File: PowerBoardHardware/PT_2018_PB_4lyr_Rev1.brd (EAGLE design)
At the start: 177.8 x 209.6 mm, 249 parts, among them J1 APP_2POS_CONFIG12V_VERT, J2 APP_2POS_CONFIG12V_VERT, J3 APP_2POS_CONFIG12V_VERT, J4 RJ45KEYSTONE-942, J5 APP_2POS_CONFIGMOCO_VERT, J6 JTAG_ARM_10PIN, Q1 Q_IRFS7437PbF, Q10 Q_IRFS7437PbF, Q11 2N7002, Q12 2N7002, Q13 2N7002PW, Q2 Q_IRFS7437PbF, Q3 Q_IRFS7437PbF, Q4 Q_IRFS7437PbF, Q5 MOSFET-NCHANNELFDD8780, Q6 Q_IRFS7437PbF, Q7 Q_IRFS7437PbF, Q8 MOSFET-NCHANNELFDD8780, Q9 Q_IRFS7437PbF, U1 ACS722LLCTR-40AU-T, U10 LT1910, U11 LT1910, U12 ACS722LLCTR-40AU-T, U13 LT1910, U14 ACS722LLCTR-40AU-T, U15 LT1910, U16 LT1910, U17 ACS722LLCTR-40AU-T, U18 ACS722LLCTR-40AU-T, U19 LT1910, U2 ACS722LLCTR-40AU-T, U20 LT1910, U21 SLVU2.8-4, U22 HX1198FNL, U23 MAX3232D, U3 LT1910, U4 ACS722LLCTR-40AU-T, U5 LT1910, U6 ACS722LLCTR-40AU-T, U7 LT1910, U8 ACS722LLCTR-40AU-T, U9 ACS722LLCTR-40AU-T, Y1 CRYATL_32K_SMD, Y2 NX3225GA

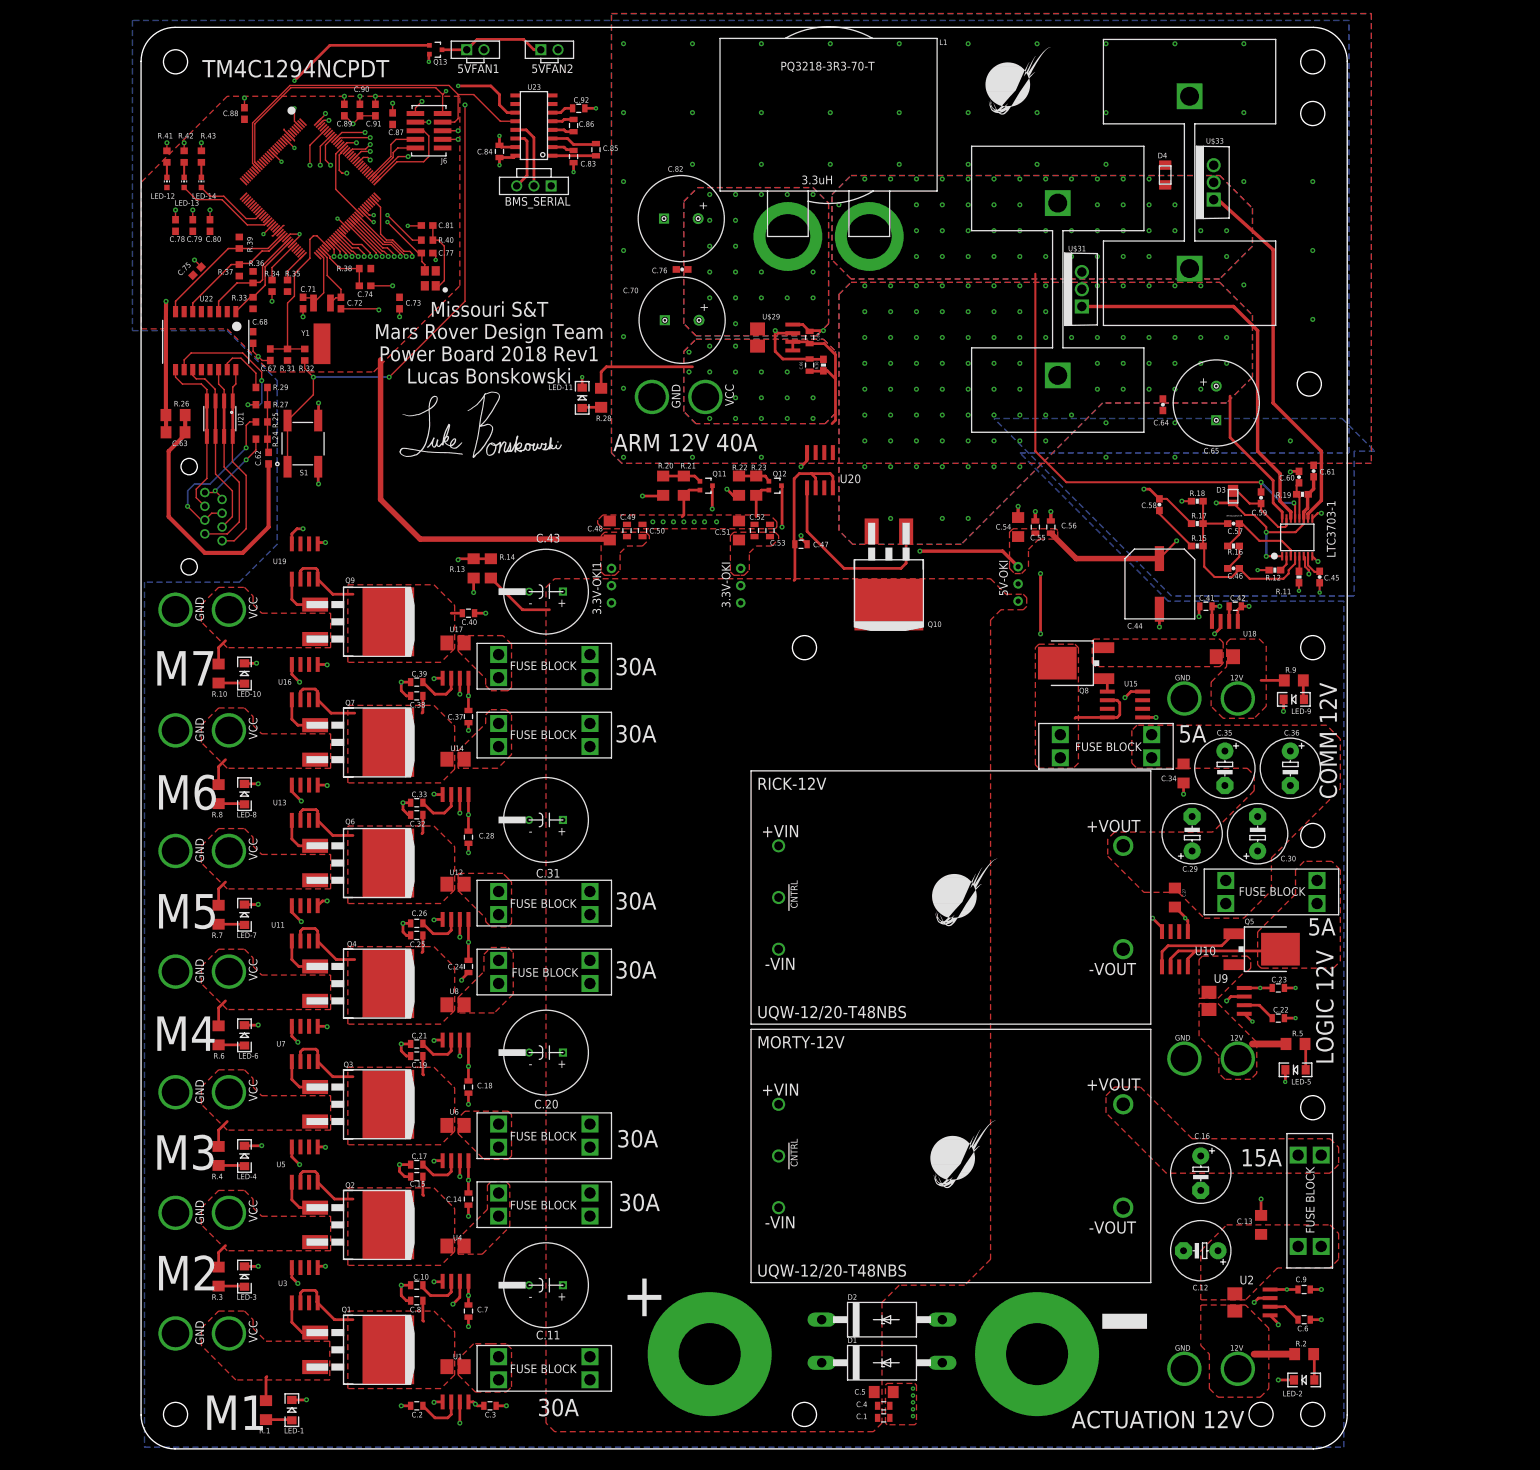
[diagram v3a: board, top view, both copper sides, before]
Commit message: Rev 2 2018
Integrated tiva/ buck converter removed.  Pack voltage arm bus added. Positive and negative terminals flipped.  Could add pin receptacles to muratas still
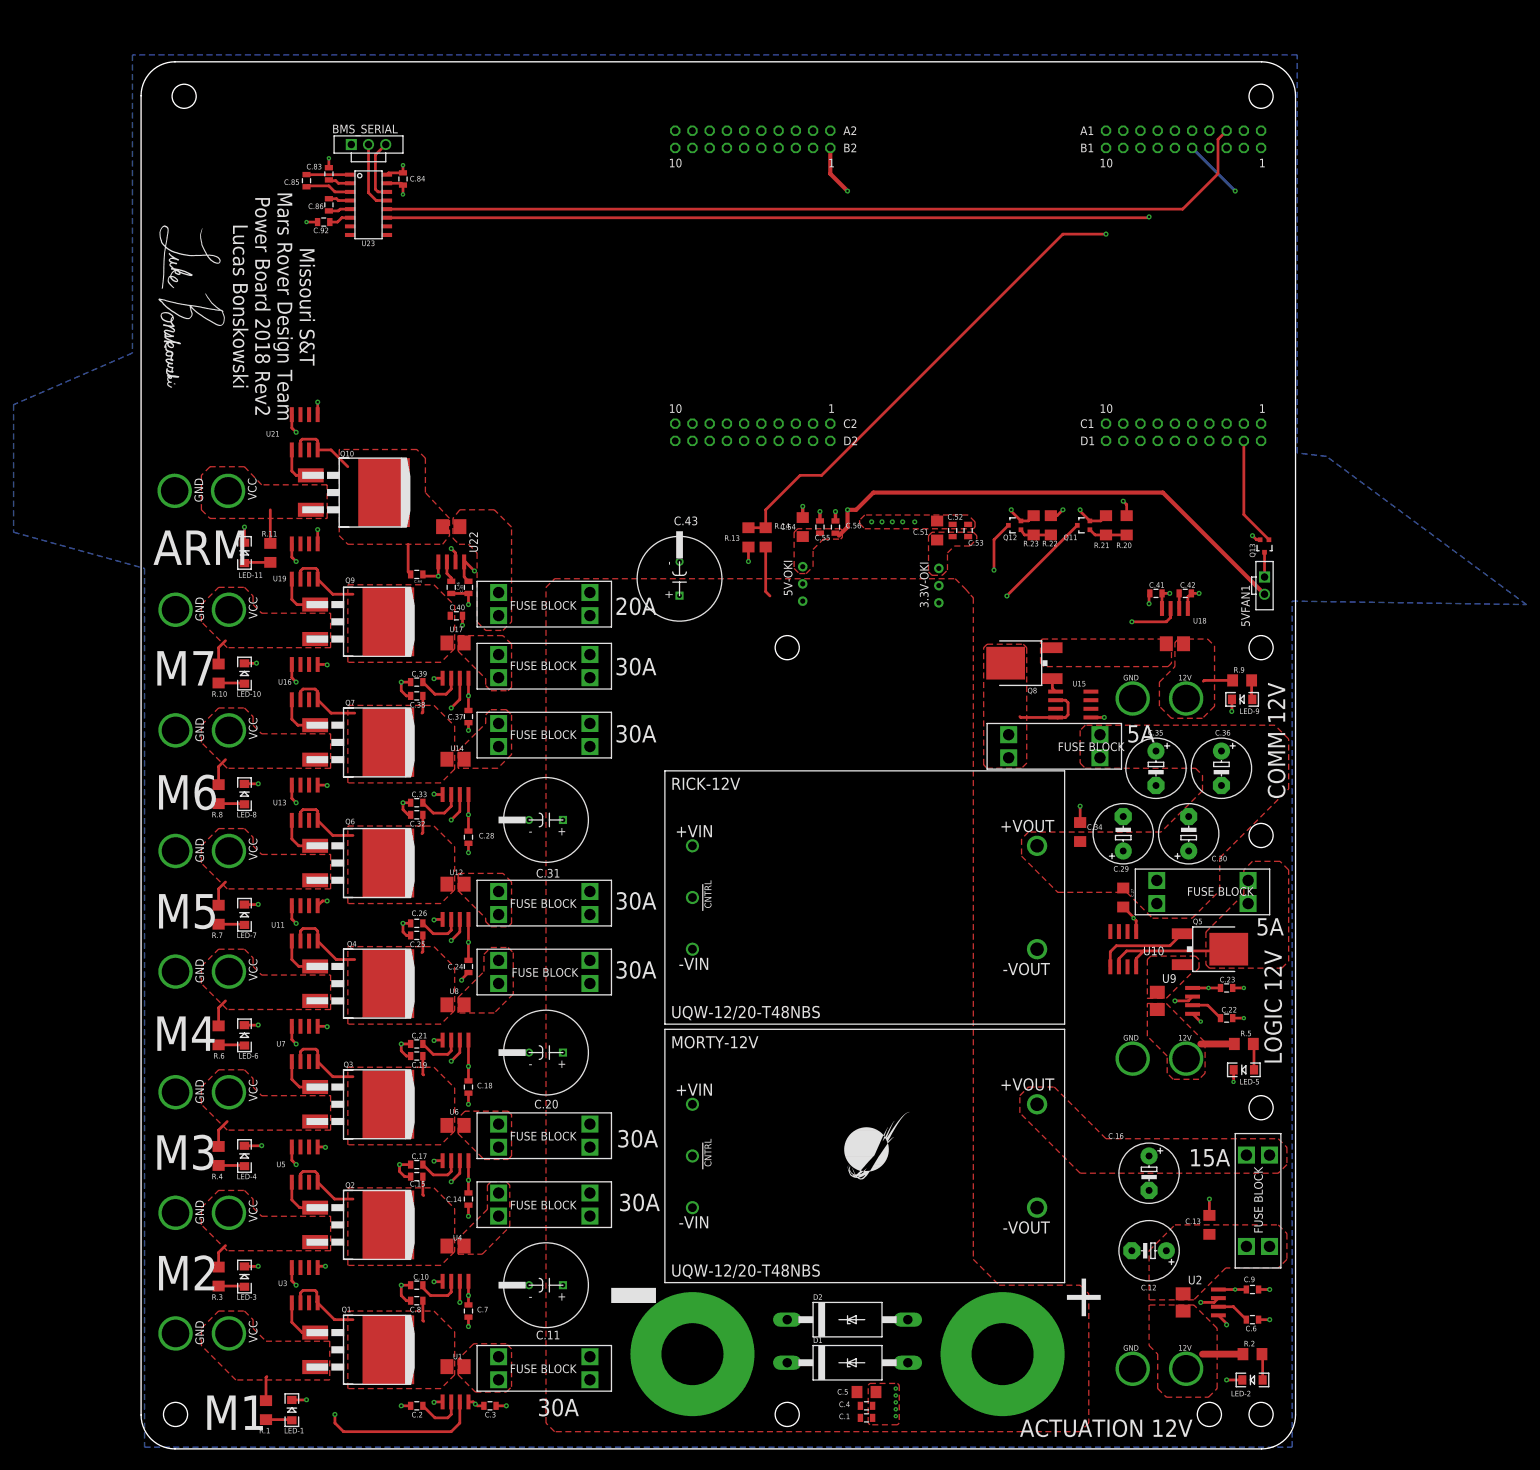
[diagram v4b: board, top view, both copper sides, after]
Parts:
- removed 3.3V-OKI1: Q_OKI-78SR, MRDT-2015-PowerBoard:OKI-78SR_HORIZ
- removed 5VFAN2: SL02, MRDT-Connectors:MOLEX-70543-0001
- removed C.47, C.69: .1µF, SparkFun-Capacitors:0805
- removed C.48: 10uF, SparkFun-Capacitors:1206
- removed C.49: 1nF, SparkFun-Capacitors:0805
- removed C.50: .1uF, SparkFun-Capacitors:0805
- removed C.57: 470p, SparkFun-Passives:0603-CAP
- removed C.58: 2200p, SparkFun-Passives:0603-CAP
- removed C.59: 0.1uF, SparkFun-Passives:0603-CAP
- removed C.60: 1uF, SparkFun-Passives:0603-CAP
- removed C.61: 10u, SparkFun-Passives:0603-CAP
- removed C.62: 1000pF, resistor:C0603
- removed C.63: 4700pF, resistor:C1206
- removed C.64: 1000p, SparkFun-Passives:0603-CAP
- removed C.65: 100u, buckconverter:CAP_POL_220UF
- removed C.66: 10n, SparkFun-Capacitors:0805
- removed C.67, C.68, C.73, C.74, C.75, C.78, C.79, C.80, C.87, C.88, C.90: 0.1uF, resistor:C0603
- removed C.70, C.82: 220u, buckconverter:CAP_POL_220UF
- removed C.71, C.72, C.77, C.81: 12pF, resistor:C0603
- removed C.76: 22p, SparkFun-Passives:0603-CAP
- removed C.89: 2.2uF, resistor:C0603
- removed C.91: 1.0uF, resistor:C0603
- removed D3: RF05VAM1STR, buckconverter:DIODE_STANDARD_100V
- removed D4: RBR3MM30ATR, buckconverter:DIODE_SCHOTTKY_30V_1A
- removed J4: RJ45KEYSTONE-942, MRDT-Connectors:KEYSTONE-942
- removed J5: APP_2POS_CONFIGMOCO_VERT, MRDT-Connectors:APP45_MOCO_VERT_CONFIG
- removed J6: JTAG_ARM_10PIN, MRDT-Connectors:CON_2X5_50MIL
- removed L1: 3.3uH, buckconverter:PLANAR_INDUCTOR_3.3UH
- removed LED-12: ORANGE, led:CHIP-LED0603
- removed LED-13, LED-14: GREEN, led:CHIP-LED0603
- removed LOGO1, U$34: MRDT_LOGO, MRDT-Hardware:MRDT_LOGO
- removed LTC3703-1: LTC3703-5, MRDT-ICs:SSOP-16
- removed R.12: 19.1k, SparkFun-Passives:0603-RES
- removed R.15, R.16, R.30: 10k, SparkFun-Passives:0603-RES
- removed R.17: 113k, SparkFun-Passives:0603-RES
- removed R.18: 8.06k, SparkFun-Passives:0603-RES
- removed R.19: 10, SparkFun-Passives:0603-RES
- removed R.24, R.25, R.27, R.29: 75, resistor:R0603
- removed R.26: 1M, resistor:R1206
- removed R.28: 1kΩ, SparkFun-Passives:1206
- removed R.31: 10k, resistor:R0603
- removed R.32: 100, resistor:R0603
- removed R.33: 49.9, rcl:R0603
- removed R.34: 4.87k 1%, resistor:R0603
- removed R.35: 1M, resistor:R0603
- removed R.36: 49.4, resistor:R0603
- removed R.37, R.39: 49.9, resistor:R0603
- removed R.38: 51, resistor:R0603
- removed R.40: 2k, resistor:R0603
- removed R.41, R.42, R.43: 330, resistor:R0603
- removed S1: SWITCH_TACTILE, MRDT-UserInput:SWITCH_6MM_6MM_TE_CON_SMD
- removed TM4C1294NCPDT: TM4C1294NCPDT, MRDT-Microcontrollers:TQFP-128
- removed U$32: 530002B02500G, buckconverter:RADIAL_FIN_HEATSINK
- removed U$33: IPP052N06L3GXKSA1, buckconverter:TO-220
- removed U$35, U$36, U$37: MOUNTING_HOLE#6, MRDT-Hardware:#6_SCREW
- removed Y1: CRYATL_32K_SMD, MRDT-Passives:CRYSTAL_32K_SMD
- removed Y2: NX3225GA, MRDT-Passives:NDK3.2X2.5
- C.44: value 22u -> .1µF; device buckconverter:CAP_POL_22UF -> SparkFun-Capacitors:0805
- C.45: value 0.1uF -> .1µF; device SparkFun-Passives:0603-CAP -> SparkFun-Capacitors:0805
- C.46: value 1000p -> 1nF; device SparkFun-Passives:0603-CAP -> SparkFun-Capacitors:0805
- R.11: value 16.5k -> 5kΩ; device SparkFun-Passives:0603-RES -> SparkFun-Passives:1206
- U$23: value MOUNTING_HOLE#6 -> APP_2POS_CONFIGMOCO_VERT; device MRDT-Hardware:#6_SCREW -> MRDT-Connectors:APP45_MOCO_VERT_CONFIG
- U$29: value MLX91210 -> ATC_FUSE_BLOCK; device buckconverter:SOIC8_ACS711 -> MRDT-Hardware:BLOCK_3557-2
- U$30: value 530002B02500G -> MOUNTING_HOLE#6; device buckconverter:RADIAL_FIN_HEATSINK -> MRDT-Hardware:#6_SCREW
- U$31: value IPP052N06L3GXKSA1 -> MOUNTING_HOLE#6; device buckconverter:TO-220 -> MRDT-Hardware:#6_SCREW
- U20: value LT1910 -> TIVA-1294; device Jake:SO8 -> MRDT-Microcontrollers:TIVA-C-CONNECTED
- U21: value SLVU2.8-4 -> LT1910; device MRDT-ICs:SOIC8 -> Jake:SO8
- U22: value HX1198FNL -> ACS722LLCTR-40AU-T; device MRDT-ICs:HX1198FNL -> MRDT-2015-PowerBoard:SOIC8_ACS711
- moved R.11 151.7 mm to (19.1, 132.1), turned to 270 degrees
- moved Q13 142.4 mm to (165.6, 133.1), turned to 180 degrees
- moved 5VFAN1 140.6 mm to (165.6, 127.3), turned to 90 degrees
- moved U$30 131.9 mm to (6.35, 199.4), turned to 0 degrees
- moved C.45 125.5 mm to (48.3, 127.0), turned to 90 degrees
- moved C.46 115.3 mm to (45.7, 127.0), turned to 270 degrees
- moved C.44 109.5 mm to (40.6, 128.9), turned to 180 degrees
- moved U$23 99.7 mm to (1.78, 145.2), turned to 270 degrees
- moved Q10 87.4 mm to (29.2, 146.1), turned to 270 degrees
- moved U$28 86.2 mm to (95.2, 118.1)
- moved R.20 68.6 mm to (145.3, 136.1), turned to 90 degrees
- moved R.21 62.5 mm to (142.2, 136.1), turned to 90 degrees
- moved U20 58.3 mm to (41.9, 139.7), turned to 0 degrees
- moved U$29 56.8 mm to (49.5, 127.9), turned to 0 degrees
- moved Q11 55.9 mm to (138.9, 136.1), turned to 90 degrees
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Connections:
- removed net !RESET: J6.P10, R.32.2, S1.P$3, S1.P$4
- removed net +3V3: 3.3V-OKI1.3, C.48.1, C.49.1, C.50.1, C.68.1, C.73.1, C.75.1, C.78.1, C.79.1, C.80.1, C.87.1, C.88.1, J6.P1, LED-12.A, R.31.1, R.33.1, R.35.2, R.36.1, R.37.1, R.38.2, R.39.1, TM4C1294NCPDT.P$101, TM4C1294NCPDT.P$113, TM4C1294NCPDT.P$122, TM4C1294NCPDT.P$16, TM4C1294NCPDT.P$26, TM4C1294NCPDT.P$28, TM4C1294NCPDT.P$39, TM4C1294NCPDT.P$47, TM4C1294NCPDT.P$51, TM4C1294NCPDT.P$52, TM4C1294NCPDT.P$69, TM4C1294NCPDT.P$7, TM4C1294NCPDT.P$79, TM4C1294NCPDT.P$8, TM4C1294NCPDT.P$9, TM4C1294NCPDT.P$90, U22.P$2, U22.P$7
- removed net ARM-BUS: J5.VCC, R.28.1, U$29.4
- removed net EN0LED0: LED-14.A, TM4C1294NCPDT.P$42
- removed net EN0LED1: LED-13.A, TM4C1294NCPDT.P$46
- removed net EN0RXI_N: R.39.2, TM4C1294NCPDT.P$53, U22.P$8
- removed net EN0RXI_P: R.37.2, TM4C1294NCPDT.P$54, U22.P$6
- removed net EN0TXO_N: R.36.2, TM4C1294NCPDT.P$56, U22.P$3
- removed net EN0TXO_P: R.33.2, TM4C1294NCPDT.P$57, U22.P$1
- removed net FAN_CTL_1: Q13.1, TM4C1294NCPDT.P$3
- removed net N$10: LTC3703-1.5, R.11.2
- removed net N$14: C.45.1, LTC3703-1.7
- removed net N$2: LED-11.A, R.28.2
- removed net N$23: C.57.1, LTC3703-1.3, R.16.2
- removed net N$24: C.46.1, R.16.1
- removed net N$26: C.58.1, R.15.1
- removed net N$27: C.46.2, C.57.2, LTC3703-1.4, R.15.2, R.17.2, R.18.1
- removed net N$29: C.60.1, LTC3703-1.12, R.19.1
- removed net N$30: LTC3703-1.10, U$33.1
- removed net N$31: C.59.2, D4.P$2, L1.P$2, LTC3703-1.13, U$31.3, U$33.2
- removed net N$32: C.59.1, D3.P$1, LTC3703-1.15
- removed net N$33: LTC3703-1.14, U$31.1
- removed net N$34: LTC3703-1.2, R.12.2
- removed net N$36: Q10.1, U20.5
- removed net N_$1: R.29.2, U22.P$15
- removed net N_$10: C.74.1, R.38.1, TM4C1294NCPDT.P$68
- removed net N_$11: J4.P$4, J4.P$5, R.25.2
- removed net N_$12: R.35.1, TM4C1294NCPDT.P$64
- removed net N_$13: J4.P$1, J4.P$2, R.24.2
- removed net N_$14: C.62.1, R.24.1, R.25.1, R.27.1, R.29.1
- removed net N_$15: C.62.2, C.63.1, R.26.2
- removed net N_$16: C.89.1, C.90.1, C.91.1, TM4C1294NCPDT.P$115, TM4C1294NCPDT.P$87
- removed net N_$17: R.40.2, TM4C1294NCPDT.P$89
- removed net N_$18: C.77.1, TM4C1294NCPDT.P$88, Y2.P$3
- removed net N_$19: R.34.2, TM4C1294NCPDT.P$59
- removed net N_$20: C.67.1, R.31.2, R.32.1, TM4C1294NCPDT.P$70
- removed net N_$21: C.81.1, R.40.1, Y2.P$1
- removed net N_$22: C.72.1, TM4C1294NCPDT.P$67, Y1.P$2
- removed net N_$23: C.71.1, TM4C1294NCPDT.P$66, Y1.P$1
- removed net N_$26: LED-12.C, R.41.1
- removed net N_$3: R.27.2, U22.P$10
- removed net N_$4: J4.P$7, U21.2, U21.7, U22.P$14
- removed net N_$5: J4.P$6, U21.3, U21.6, U22.P$11
- removed net N_$6: J4.P$8, U21.1, U21.8, U22.P$16
- removed net N_$7: J4.P$3, U21.4, U21.5, U22.P$9
- removed net N_$8: LED-13.C, R.42.1
- removed net N_$9: LED-14.C, R.43.1
- removed net TARGET_TCK/SWCLK: J6.P4, TM4C1294NCPDT.P$100
- removed net TARGET_TDI: J6.P8, TM4C1294NCPDT.P$98
- removed net TARGET_TDO/SWO: J6.P6, TM4C1294NCPDT.P$97
- removed net TARGET_TMS/SWDIO: J6.P2, TM4C1294NCPDT.P$99
- removed net VOUT12+: C.58.2, C.70.+, C.76.1, C.82.+, L1.P$1, R.17.1, U$29.1
- new net DRAIN-ARM: C.44.2, Q10.TAB, U21.6, U21.8, U22.4
- new net FAN-CTL: Q13.1, U20.PM3
- new net FILTER-ARM: C.46.1, U22.6
- new net GATE-ARM: Q10.1, U21.5
- new net LEDLINE-ARM: LED-11.A, R.11.2
- new net SIG-LOGIC: U20.PH2
- new net V_BATT_ARM: U$29.OUT_1, U$29.OUT_2, U22.1
- net 12V-AUX-COM: now also J3.VCC, R.9.1, U18.4; no longer J2.VCC, R.5.1, U9.4
- net 12V-AUX-LOGIC: now also J2.VCC, R.5.1, U9.4; no longer J3.VCC, R.9.1, U18.4
- net 3.3V: now also C.45.2, U20.+3V3_1, U20.+3V3_2, U22.8
- net 5V: now also U20.+5V_1, U20.+5V_2; no longer 5VFAN2.2, C.44.+, C.61.1, C.69.2, D3.P$2, LTC3703-1.1, LTC3703-1.11, R.19.2, U$29.8
- net ACT-CTL: now also U20.PN3; no longer TM4C1294NCPDT.P$109
- net COM-SIG: no longer TM4C1294NCPDT.P$118
- net GND: now also C.44.1, C.45.1, C.46.2, U$23.GND, U20.GND_1, U20.GND_2, U20.GND_3, U20.GND_4, U21.1, U22.5; no longer 3.3V-OKI1.2, C.44.-, C.45.2, C.47.1, C.48.2, C.49.2, C.50.2, C.60.2, C.61.2, C.63.2, C.64.2, C.65.GND, C.66.2, C.67.2, C.68.2, C.69.1, C.70.GND, C.71.2, C.72.2, C.73.2, C.74.2, C.75.2, C.76.2, C.77.2, C.78.2, C.79.2, C.80.2, C.81.2, C.82.GND, C.87.2, C.88.2, C.89.2, C.90.2, C.91.2, D4.P$1, J5.GND, J6.P3, J6.P5, LTC3703-1.6, LTC3703-1.8, LTC3703-1.9, R.11.1, R.12.1, R.18.2, R.26.1, R.30.1, R.34.1, R.41.2, R.42.2, R.43.2, S1.P$1, S1.P$2, TM4C1294NCPDT.P$10, TM4C1294NCPDT.P$114, TM4C1294NCPDT.P$17, TM4C1294NCPDT.P$48, TM4C1294NCPDT.P$55, TM4C1294NCPDT.P$58, TM4C1294NCPDT.P$80, U$29.5, U$29.6, U$33.3, U20.1
- net IMEAS-ACT: now also U20.PE2; no longer TM4C1294NCPDT.P$107
- net IMEAS-ARM: now also U20.PD0, U22.7; no longer C.66.1, R.30.2, TM4C1294NCPDT.P$128, U$29.7
- net IMEAS-COM: now also U20.PE1; no longer TM4C1294NCPDT.P$119
- net IMEAS-LOGIC: now also U20.PE0; no longer TM4C1294NCPDT.P$121
- net IMEAS-M1: now also U20.PK3; no longer TM4C1294NCPDT.P$71
- net IMEAS-M2: now also U20.PK2; no longer TM4C1294NCPDT.P$72
- net IMEAS-M3: now also U20.PK1; no longer TM4C1294NCPDT.P$73
- net IMEAS-M4: now also U20.PK0; no longer TM4C1294NCPDT.P$74
- net IMEAS-M5: now also U20.PB5; no longer TM4C1294NCPDT.P$75
- net IMEAS-M6: now also U20.PB4; no longer TM4C1294NCPDT.P$76
- net IMEAS-M7: now also U20.PE3; no longer TM4C1294NCPDT.P$77
- net LOGIC-SIG: no longer TM4C1294NCPDT.P$120
- net LOGIC/COM-CTL: now also U20.PP2; no longer TM4C1294NCPDT.P$112
- net N$5: no longer 5VFAN2.1
- net SER_RX: now also U20.PC4; no longer J6.P7, TM4C1294NCPDT.P$25
- net SER_TX: now also U20.PC5; no longer J6.P9, TM4C1294NCPDT.P$24
- net SIG-ARM: now also U20.PK5, U21.4; no longer TM4C1294NCPDT.P$127, U20.4
- net SIG-M1: now also U20.PK7; no longer TM4C1294NCPDT.P$94
- net SIG-M2: now also U20.PK6; no longer TM4C1294NCPDT.P$86
- net SIG-M3: now also U20.PH1; no longer TM4C1294NCPDT.P$85
- net SIG-M4: now also U20.PH0; no longer TM4C1294NCPDT.P$84
- net SIG-M5: now also U20.PM2; no longer TM4C1294NCPDT.P$83
- net SIG-M6: now also U20.PM1; no longer TM4C1294NCPDT.P$82
- net SIG-M7: now also U20.PM0; no longer TM4C1294NCPDT.P$81
- net SOURCE-ARM: now also R.11.1, U$23.VCC; no longer C.64.1, C.65.+, LTC3703-1.16, U$31.2
- net VMEAS-VBATT: now also U20.PE5; no longer TM4C1294NCPDT.P$124
- net V_BATT: now also U$29.IN_1, U$29.IN_2; no longer 3.3V-OKI1.1, C.47.2, Q10.TAB, U20.6, U20.8
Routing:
- net LOGIC-SIG: track 220.7 -> 0.00 mm, vias 2 -> 0
- net COM-SIG: track 202.7 -> 0.00 mm, vias 2 -> 0
- net 5V: track 250.8 -> 127.5 mm, vias 6 -> 2
- net GND: track 252.4 -> 141.6 mm, vias 156 -> 75
- net IMEAS-LOGIC: track 247.4 -> 138.2 mm, vias 2 -> 1
- net IMEAS-M7: track 86.3 -> 192.4 mm, vias 2 -> 1
- net IMEAS-COM: track 186.2 -> 81.9 mm, vias 2 -> 1
- net IMEAS-ACT: track 280.8 -> 178.8 mm, vias 4 -> 2
- net LOGIC/COM-CTL: track 98.7 -> 14.9 mm, vias 2 -> 1
- net !RESET: track 82.4 -> 0.00 mm, vias 4 -> 0
- net VOUT12+: track 77.9 -> 0.00 mm, vias 20 -> 0
- net SER_TX: track 53.4 -> 128.8 mm, vias 2 -> 1
- net SER_RX: track 56.3 -> 131.6 mm
- net ACT-CTL: track 86.3 -> 11.2 mm, vias 2 -> 1
- net N$31: track 71.2 -> 0.00 mm, vias 48 -> 0
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- added copper zone on layer 1, net DRAIN-ARM
- added copper zone on layer 1, net V_BATT_ARM
- removed copper zone on layer 1, net +3V3
- removed copper zone on layer 1, net ARM-BUS
- removed copper zone on layer 15, net ARM-BUS
- removed copper zone on layer 16, net ARM-BUS
- removed copper zone on layer 2, net ARM-BUS
- removed copper zone on layer 15, net GND
- removed copper zone on layer 2, net GND
- removed copper zone on layer 1, net N$31
- removed copper zone on layer 15, net N$31
- removed copper zone on layer 16, net N$31
- removed copper zone on layer 2, net N$31
- removed copper zone on layer 15, net SOURCE-ARM
- removed copper zone on layer 16, net SOURCE-ARM
- removed copper zone on layer 2, net SOURCE-ARM
- removed copper zone on layer 1, net VOUT12+
- removed copper zone on layer 15, net VOUT12+
- removed copper zone on layer 16, net VOUT12+
- removed copper zone on layer 2, net VOUT12+
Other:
- board size 177.8 x 209.6 mm -> 170.2 x 204.5 mm
- board text added: "20A"
- board text added: "ARM"
- board text added: "Missouri S&T Mars Rover Design Team Power Board 2018 Rev2 Lucas Bonskowski"
- board text removed: "ARM 12V 40A"
- board text removed: "Missouri S&T Mars Rover Design Team Power Board 2018 Rev1 Lucas Bonskowski"
